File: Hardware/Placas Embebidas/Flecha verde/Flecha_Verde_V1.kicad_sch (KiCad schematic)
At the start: 29 parts, among them J3 Encoder Derecho, J4 Encoder Izquierdo, J5 Distancia_Der, J6 Distancia_Izq, J7 Distancia_Frontal, J8 IN, J9 UART, SW1 SW_Push, SW2 SW_SPDT, U1 ESP32-WROOM-32E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

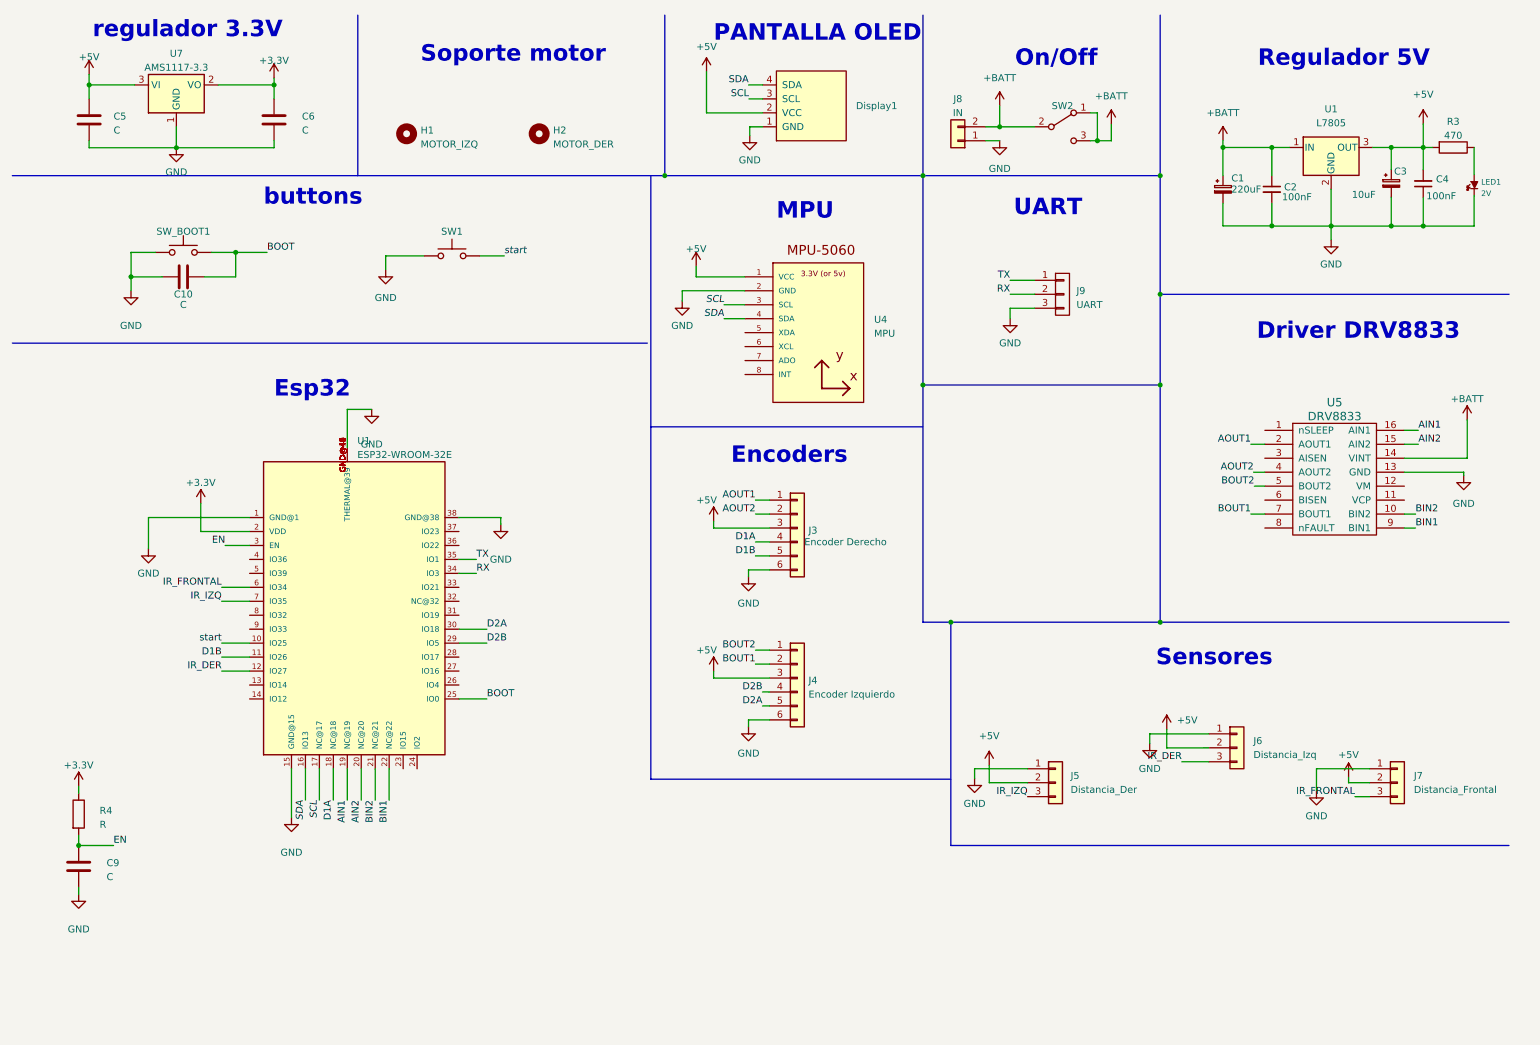
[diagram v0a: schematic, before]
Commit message: cambie ordenes en el sch y agregue carpeta img
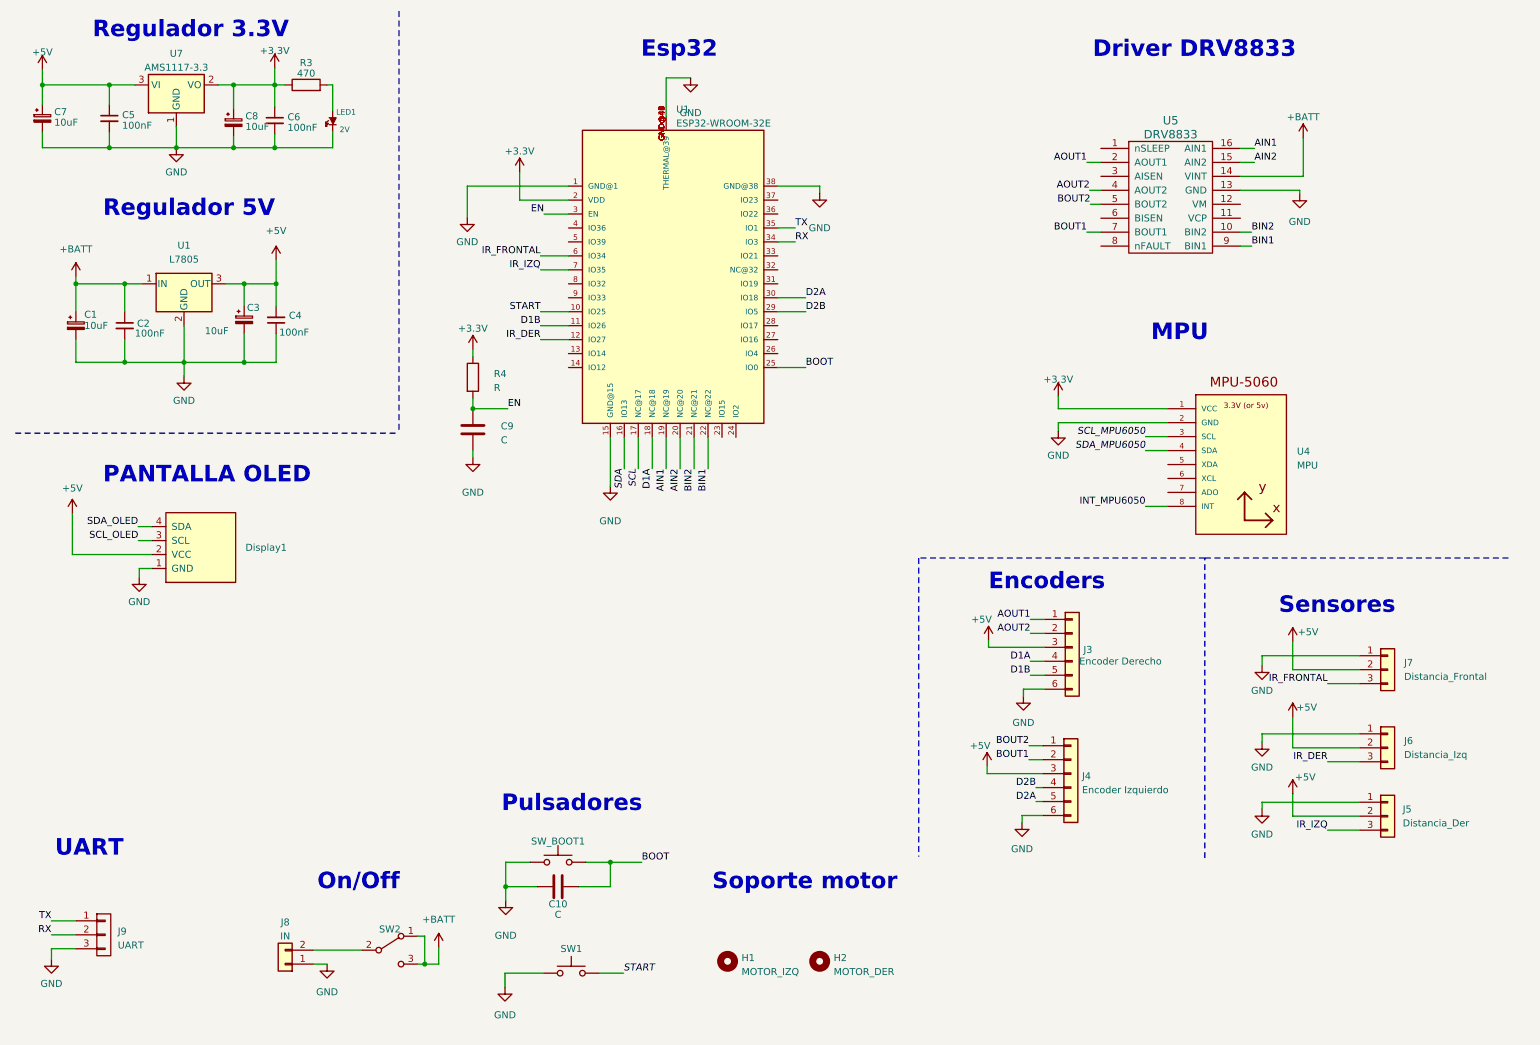
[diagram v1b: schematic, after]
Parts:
- removed C5, C6: C, EESTN5:C_1206, symbol Device:C
- added C5, C6: 100nF, symbol Device:C_Small
- added C7, C8: 10uF, symbol Device:C_Polarized_Small
- C1: value 220uF -> 10uF
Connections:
- net +3.3V: now also R3.1, U4.1 (VCC), C6.1, C8.1
- net +5V: now also C5.1, C7.1; no longer R3.2, U4.1 (VCC)
- net +BATT: no longer J8.2 (Pin_2), SW2.2 (B)
- net GND: now also C5.2, C6.2, C7.2, C8.2
- net SCL: no longer Display1.3 (SCL), U4.3 (SCL)
- net SDA: no longer Display1.4 (SDA), U4.4 (SDA)
- net at LED1.1 (A): now also R3.2; no longer R3.1
- net INT_MPU6050: now reaches U4.8 (INT)
- net start renamed START
- new net: J8.2 (Pin_2), SW2.2 (B)
- new net SCL_MPU6050: U4.3 (SCL)
- new net SCL_OLED: Display1.3 (SCL)
- new net SDA_MPU6050: U4.4 (SDA)
- new net SDA_OLED: Display1.4 (SDA)
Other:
- note added: "Pulsadores"
- note added: "Regulador 3.3V"
- note removed: "buttons"
- note removed: "regulador 3.3V"
- moved on the sheet: C1, C10, C2, C3, C4, C9, Display1, H1, H2, J3, J4, J5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

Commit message: buscando poner todo a 3.3v, y cambiando pines del esp32
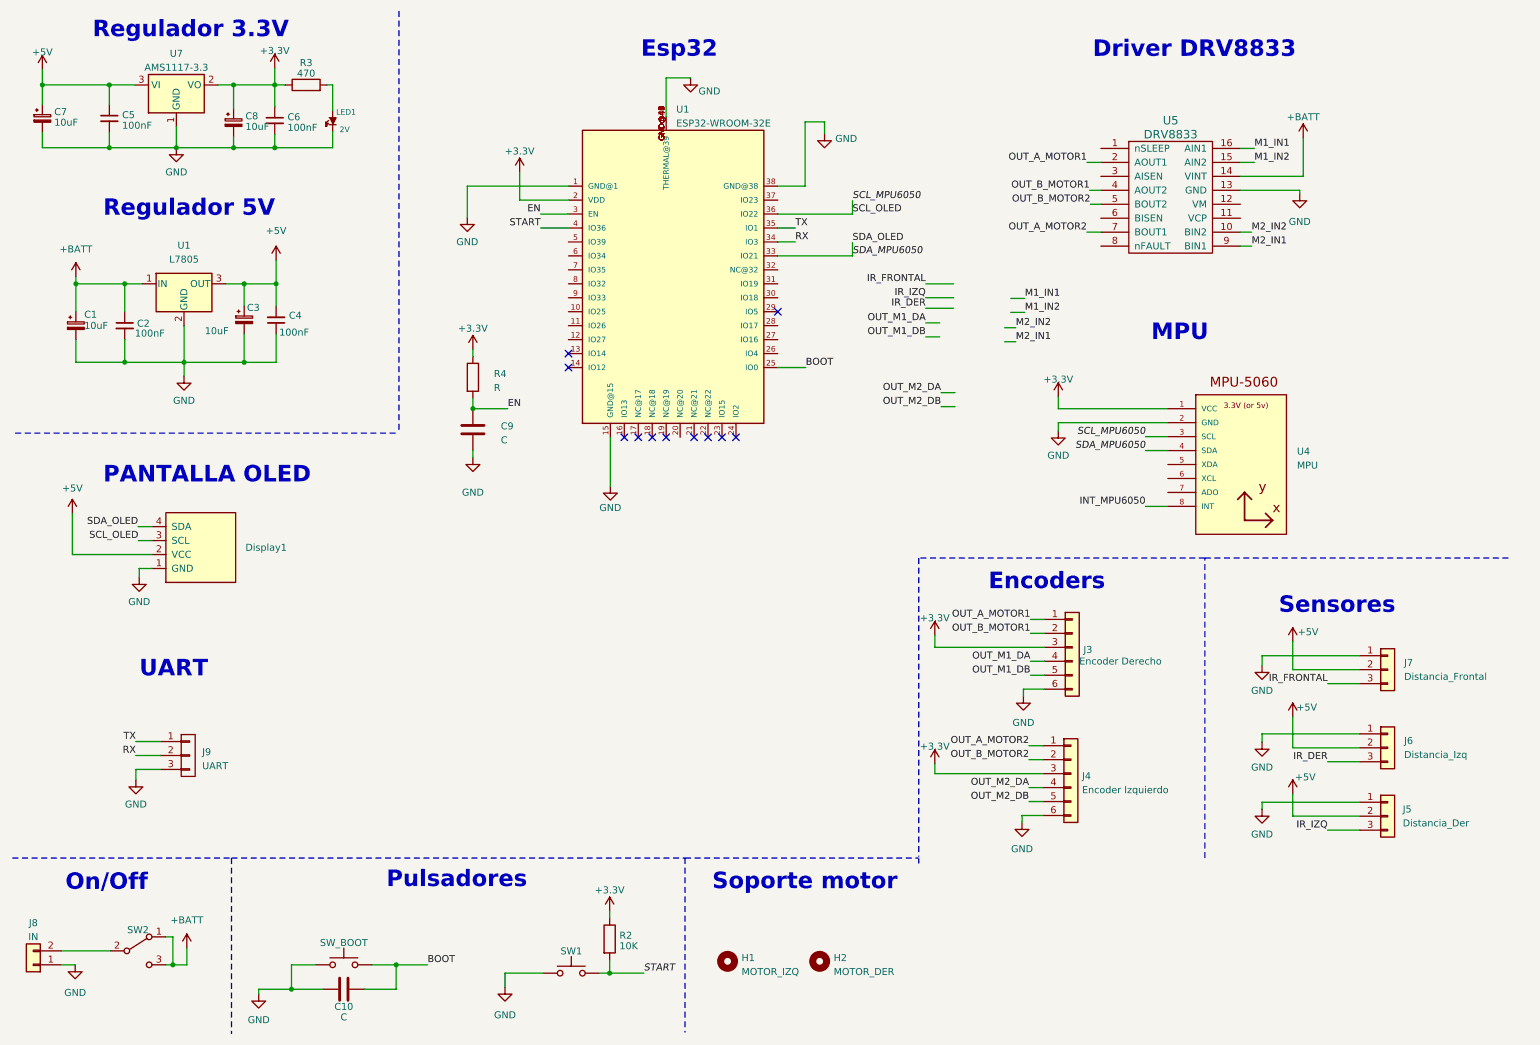
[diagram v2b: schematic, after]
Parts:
- added R2: 10K, EESTN5:R_1206, symbol Device:R
- renumbered SW_BOOT1 to SW_BOOT
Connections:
- net SCL_OLED is gone; now on net SCL_MPU6050: Display1.3 (SCL)
- net SDA_OLED is gone; now on net SDA_MPU6050: Display1.4 (SDA)
- net +3.3V: now also J3.3 (Pin_3), J4.3 (Pin_3), R2.1
- net +5V: no longer J3.3 (Pin_3), J4.3 (Pin_3)
- net IR_DER: no longer U1.12 (IO27)
- net IR_FRONTAL: no longer U1.6 (IO34)
- net IR_IZQ: no longer U1.7 (IO35)
- net SCL_MPU6050: now also U1.36 (IO22)
- net SDA_MPU6050: now also U1.33 (IO21)
- net START: now also U1.4 (IO36), R2.2; no longer U1.10 (IO25)
- net AIN1: no longer names the net of U1.19 (NC@19)
- net AIN1: no longer U5.16 (AIN1)
- net AIN2: no longer names the net of U1.20 (NC@20)
- net AIN2: no longer U5.15 (AIN2)
- net AOUT1 renamed OUT_A_MOTOR1
- net AOUT2 renamed OUT_B_MOTOR1
- net BIN1: no longer names the net of U1.22 (NC@22)
- net BIN1: no longer U5.9 (BIN1)
- net BIN2: no longer names the net of U1.21 (NC@21)
- net BIN2: no longer U5.10 (BIN2)
- net BOUT1 renamed OUT_A_MOTOR2
- net OUT_A_MOTOR2: now also J4.1 (Pin_1); no longer J4.2 (Pin_2)
- net BOUT2 renamed OUT_B_MOTOR2
- net OUT_B_MOTOR2: now also J4.2 (Pin_2); no longer J4.1 (Pin_1)
- net D1A: no longer names the net of U1.18 (NC@18)
- net D1A: no longer J3.4 (Pin_4)
- net D1B: no longer names the net of U1.11 (IO26)
- net D1B: no longer J3.5 (Pin_5)
- net D2A: no longer names the net of U1.30 (IO18)
- net D2A: no longer J4.5 (Pin_5)
- net D2B: no longer names the net of U1.29 (IO5)
- net D2B: no longer J4.4 (Pin_4)
- net SCL: no longer names the net of U1.17 (NC@17)
- net SDA: no longer names the net of U1.16 (IO13)
- new net M1_IN1: U5.16 (AIN1)
- new net M1_IN2: U5.15 (AIN2)
- new net M2_IN1: U5.9 (BIN1)
- new net M2_IN2: U5.10 (BIN2)
- new net OUT_M1_DA: J3.4 (Pin_4)
- new net OUT_M1_DB: J3.5 (Pin_5)
- new net OUT_M2_DA: J4.4 (Pin_4)
- new net OUT_M2_DB: J4.5 (Pin_5)
- no-connect marks 0 -> 11
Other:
- moved on the sheet: C10, J8, J9, SW2, SW_BOOT

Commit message: realice el sch del drv8833, me quedan dudas de pines la verdad
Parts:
- removed J9: UART, EESTN5:Pin_Header_3, symbol EESTN5:CONN_01X03
- removed SW2: SW_SPDT, Button_Switch_THT:SW_Slide_1P2T_CK_OS102011MS2Q, symbol EESTN5:SW_SPDT
- added C11: 10nF, symbol Device:C_Small
- added C12: 2,2uF, symbol Device:C_Small
- added C13: 10uF, symbol Device:C_Small
- added J2: Jumper, symbol Connector_Generic:Conn_01x03
- added J3: Conn_01x05, symbol Connector_Generic:Conn_01x05
- added R3: 47K, EESTN5:R_1206, symbol Device:R
- J8: value IN -> 7.4v
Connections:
- net +3.3V: now also U5.14 (VINT), C12.2, J3.5 (Pin_5), R3.1
- net +5V: no longer C5.1, C7.1, U7.3 (VI)
- net +BATT: now also C5.1, C7.1, U5.12 (VM), U7.3 (VI), C11.1, C13.2, J2.1 (Pin_1), J2.2 (Pin_2); no longer U5.14 (VINT)
- net GND: now also C12.1, C13.1, J3.4 (Pin_4)
- net IR_DER: now also U1.28 (IO17)
- net IR_FRONTAL: now also U1.31 (IO19)
- net IR_IZQ: now also U1.30 (IO18)
- net RX: now also J3.2 (Pin_2)
- net TX: now also J3.1 (Pin_1)
- net at J8.2 (Pin_2): now also J2.3 (Pin_3)
- net at U5.1 (nSLEEP): now also R3.2
- net at U5.11 (VCP): now also C11.2
- net NFAULT: now reaches U5.8 (nFAULT)
- no-connect marks 11 -> 17
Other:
- moved on the sheet: U5

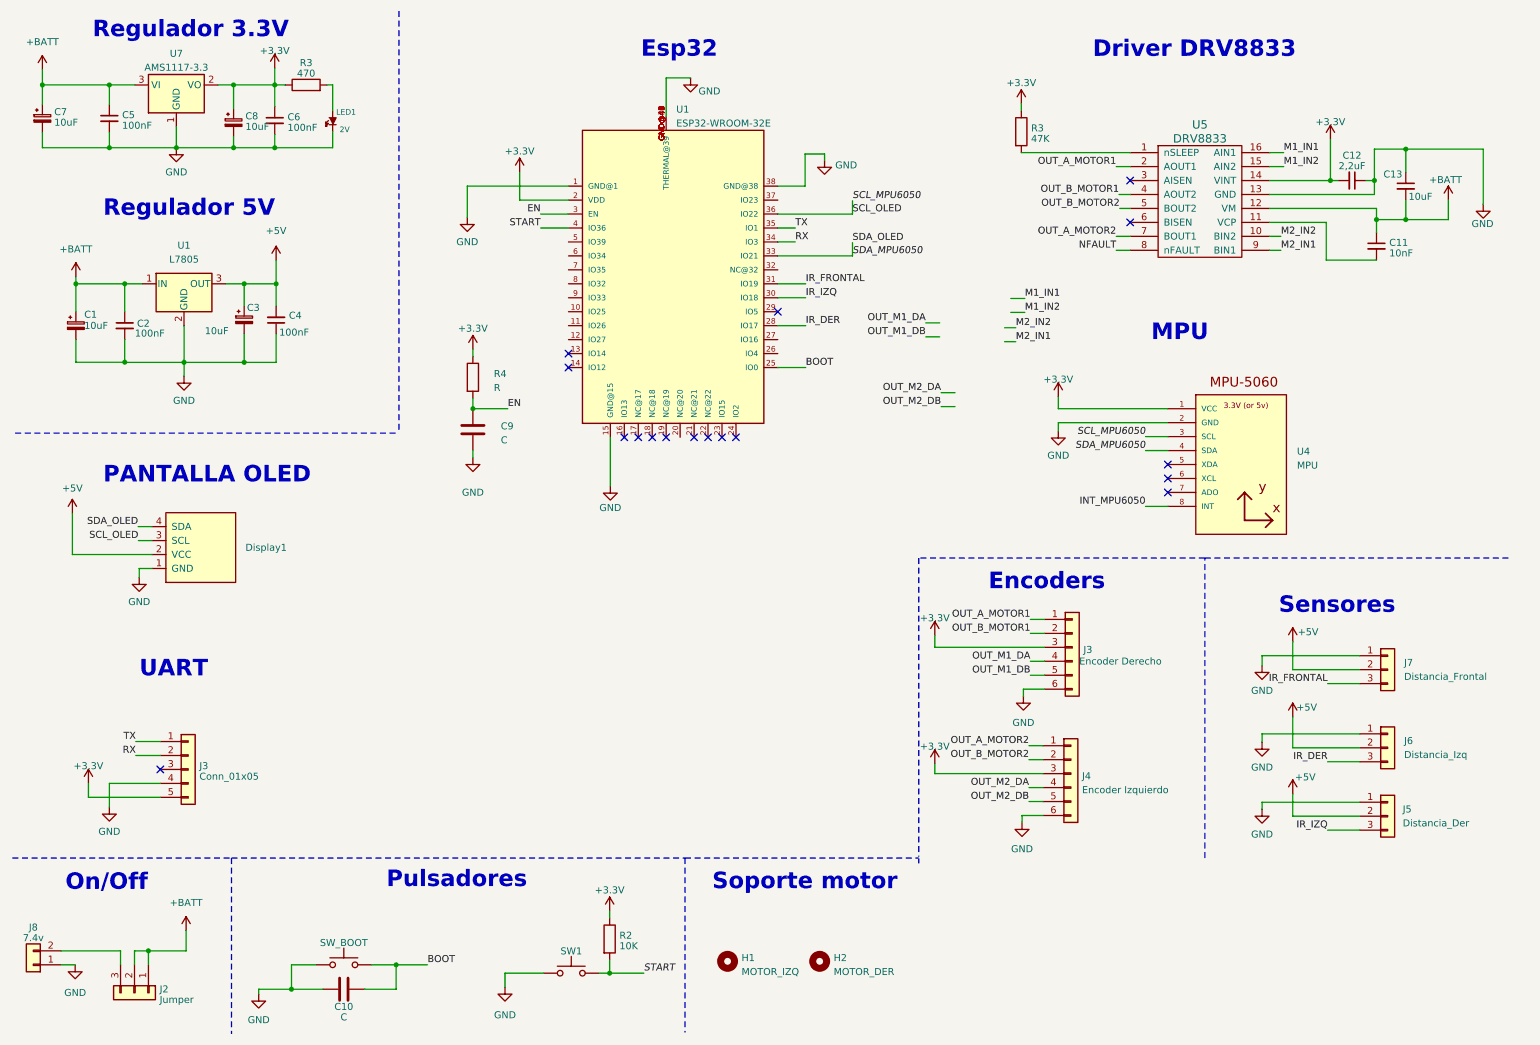
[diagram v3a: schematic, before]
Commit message: PUSE PINES SON TODOS FLEXIBLES MENOS LA COMUNICACION I2C, ESTAN RECOMENDADOS Y SON LOS USADOS SIN PROBLEMAS
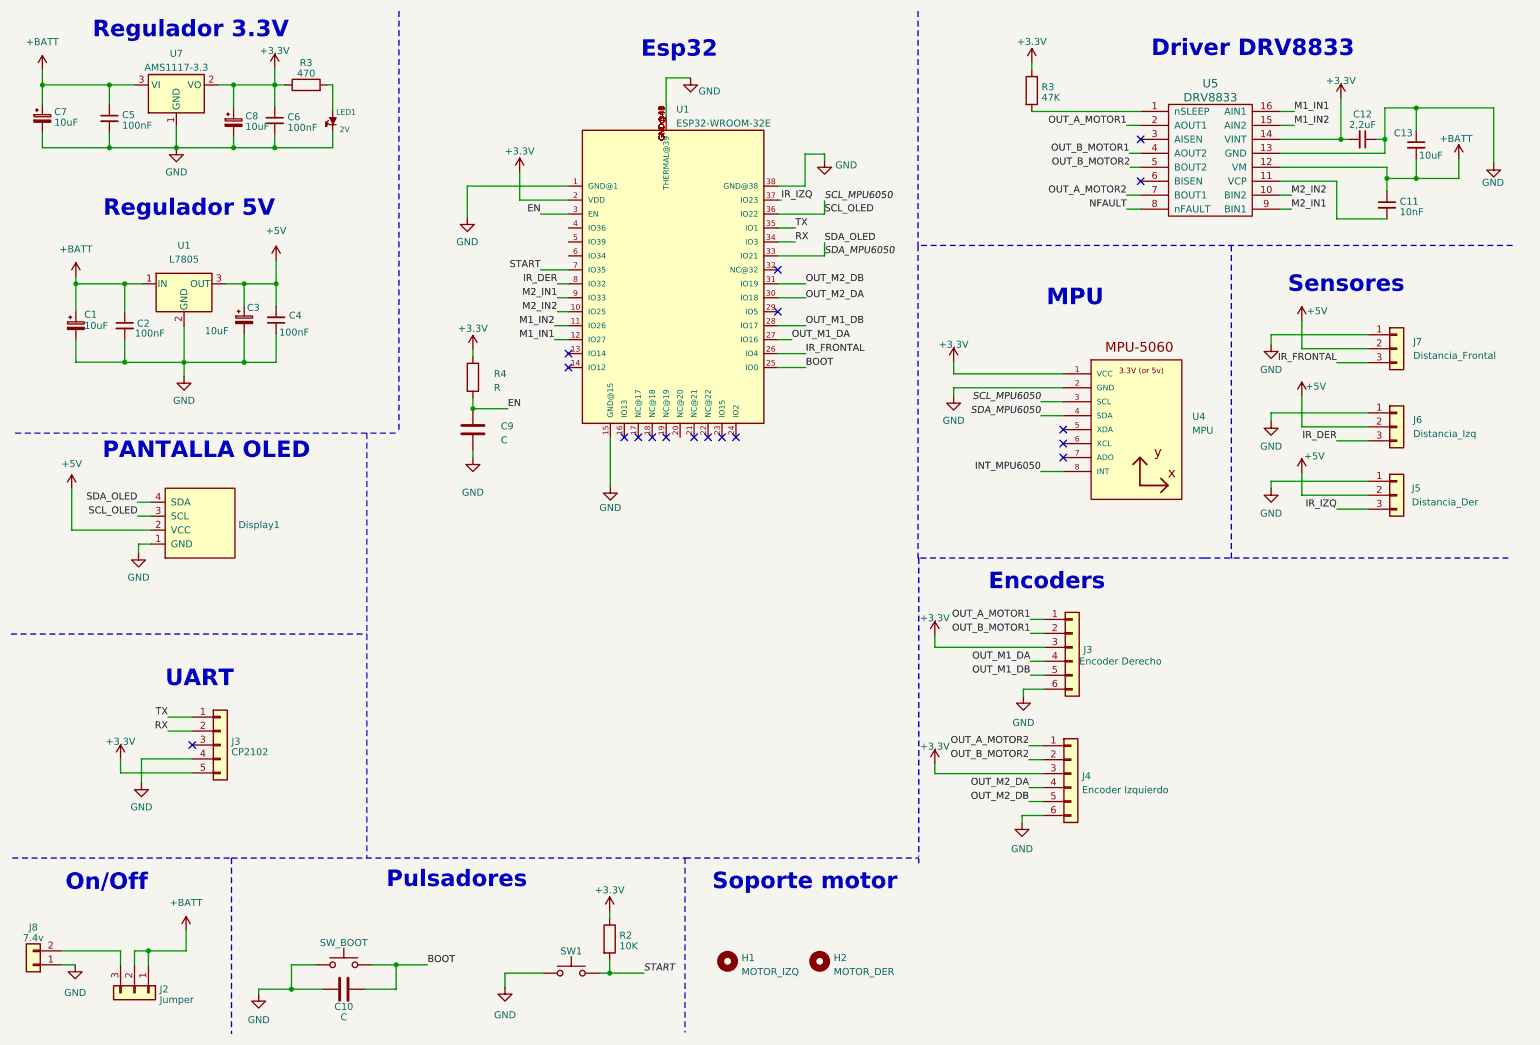
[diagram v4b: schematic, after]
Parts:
- J3: value Conn_01x05 -> CP2102
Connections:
- net IR_DER: now also U1.8 (IO32); no longer U1.28 (IO17)
- net IR_FRONTAL: now also U1.26 (IO4); no longer U1.31 (IO19)
- net IR_IZQ: now also U1.37 (IO23); no longer U1.30 (IO18)
- net M1_IN1: now also U1.12 (IO27)
- net M1_IN2: now also U1.11 (IO26)
- net M2_IN1: now also U1.9 (IO33)
- net M2_IN2: now also U1.10 (IO25)
- net OUT_M1_DA: now also U1.27 (IO16)
- net OUT_M1_DB: now also U1.28 (IO17)
- net OUT_M2_DB: now also U1.31 (IO19)
- net START: now also U1.7 (IO35); no longer U1.4 (IO36)
- no-connect marks 17 -> 18
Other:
- moved on the sheet: C11, C12, C13, Display1, J3, J5, J6, J7, R3, U4, U5

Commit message: Hice cambios simples
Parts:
- removed Display1: SSD1306-SSD1306-128x64_OLED, EESTN5:128x64OLED, symbol EESTN5:SSD1306-SSD1306-128x64_OLED
- added R5: 10K, EESTN5:R_1206, symbol Device:R
- C9: value C -> 100nF
- R4: value R -> 10k
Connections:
- net +3.3V: now also R5.1
- net BOOT: now also R5.2
- net OUT_M2_DA: now also U1.30 (IO18)
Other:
- note removed: "PANTALLA OLED"
- moved on the sheet: J3, J4
